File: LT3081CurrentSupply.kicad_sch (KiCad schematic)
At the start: 29 parts, among them J1 PosIMon, J2 PosTempMon, J3 V_{IN}, J4 V_{LED}, U1 LT3081-DPAK-7

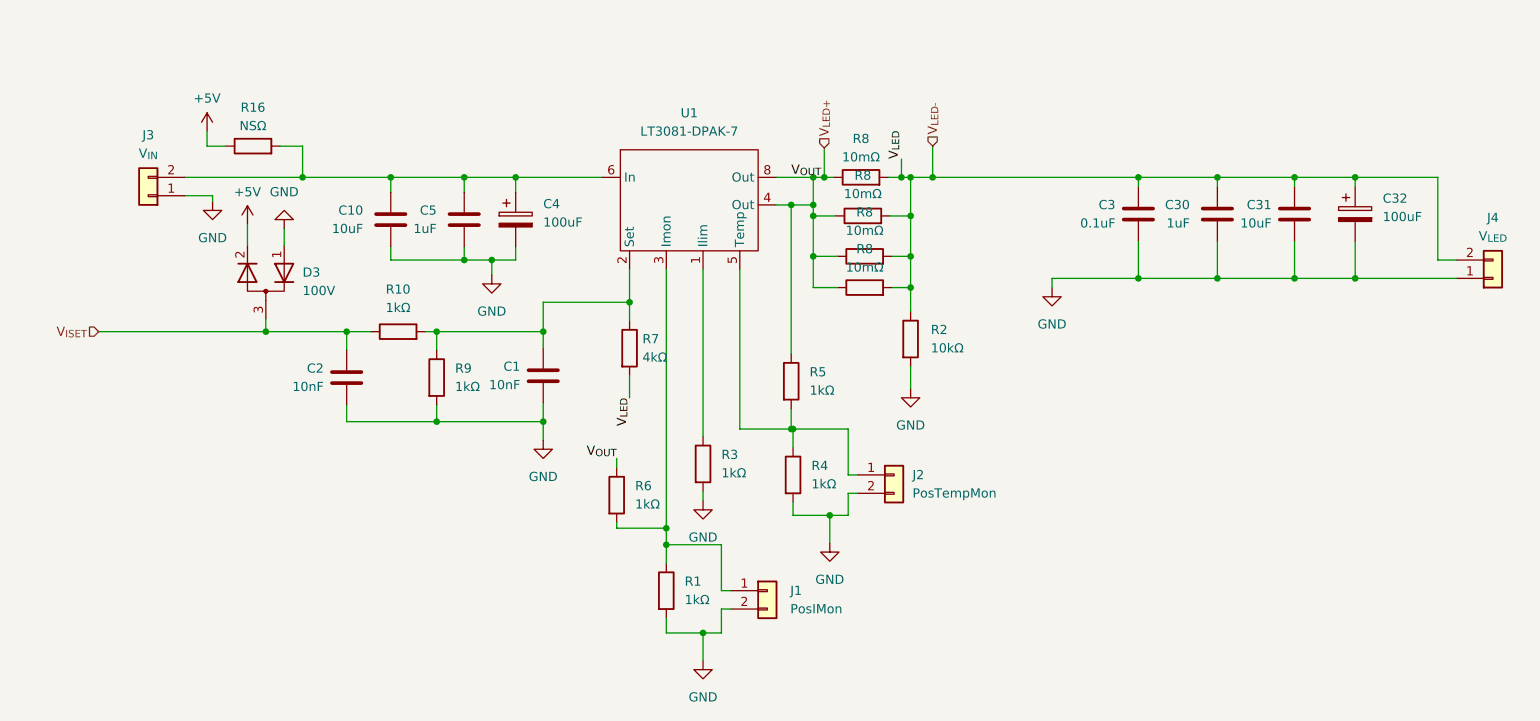
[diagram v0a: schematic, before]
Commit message: Added extra capacitor and reroute the power to better optimize the board.
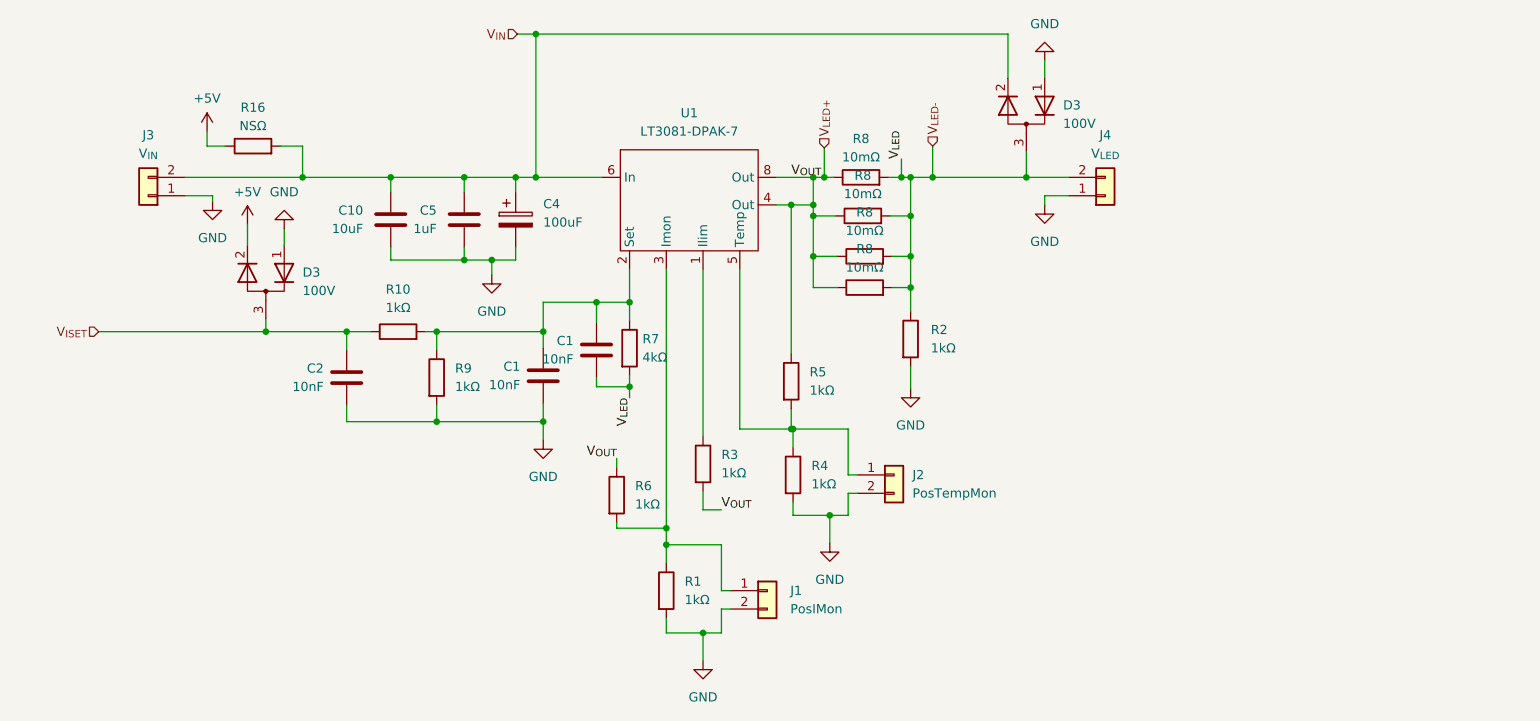
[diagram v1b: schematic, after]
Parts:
- removed C3: 0.1uF, Capacitor_SMD:C_0805_2012Metric_Pad1.18x1.45mm_HandSolder, symbol Device:C
- removed C30: 1uF, Capacitor_SMD:C_0805_2012Metric_Pad1.18x1.45mm_HandSolder, symbol Device:C
- removed C31: 10uF, Capacitor_SMD:C_0805_2012Metric_Pad1.18x1.45mm_HandSolder, symbol Device:C
- removed C32: 100uF, Capacitor_SMD:CP_Elec_8x10.5, symbol Device:C_Polarized
- added C1: 10nF, Capacitor_SMD:C_0805_2012Metric_Pad1.18x1.45mm_HandSolder, symbol Device:C
- added D3: 100V, Package_TO_SOT_SMD:SOT-23-3, symbol Device:D_Dual_Series_AKC_Parallel
- R2: value 10kΩ -> 1kΩ
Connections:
- net GND: now also D3.1 (K); no longer R3.2
- net V_{LED+}: now also R3.2
- net V_{LED-}: now also C1.2, D3.3 (A)
- net at C1.1, R10.2, R7.1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: now also C1.1
- net V_{IN}: now reaches C10.2, C4.1, C5.2, J3.2 (Pin_2), R16.2, U1.6 (In)
- net V_{IN}: now also D3.2 (K)
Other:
- moved on the sheet: J4
